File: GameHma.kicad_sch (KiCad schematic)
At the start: 15 parts, among them J1 Screw_Terminal_01x02, J2 Motor_Terminal_01x04, J3 Motor_Terminal_01x04, J4 Motor_Terminal_01x04, J5 Motor_Terminal_01x04, U1 ESP32-DEVKIT-V1, U2 A4988_STEPPER_MOTOR_DRIVER_CA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, U3 A4988_STEPPER_MOTOR_DRIVER_CA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, U4 A4988_STEPPER_MOTOR_DRIVER_CA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, U5 A4988_STEPPER_MOTOR_DRIVER_CA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, U6 SRT_MP1584EN

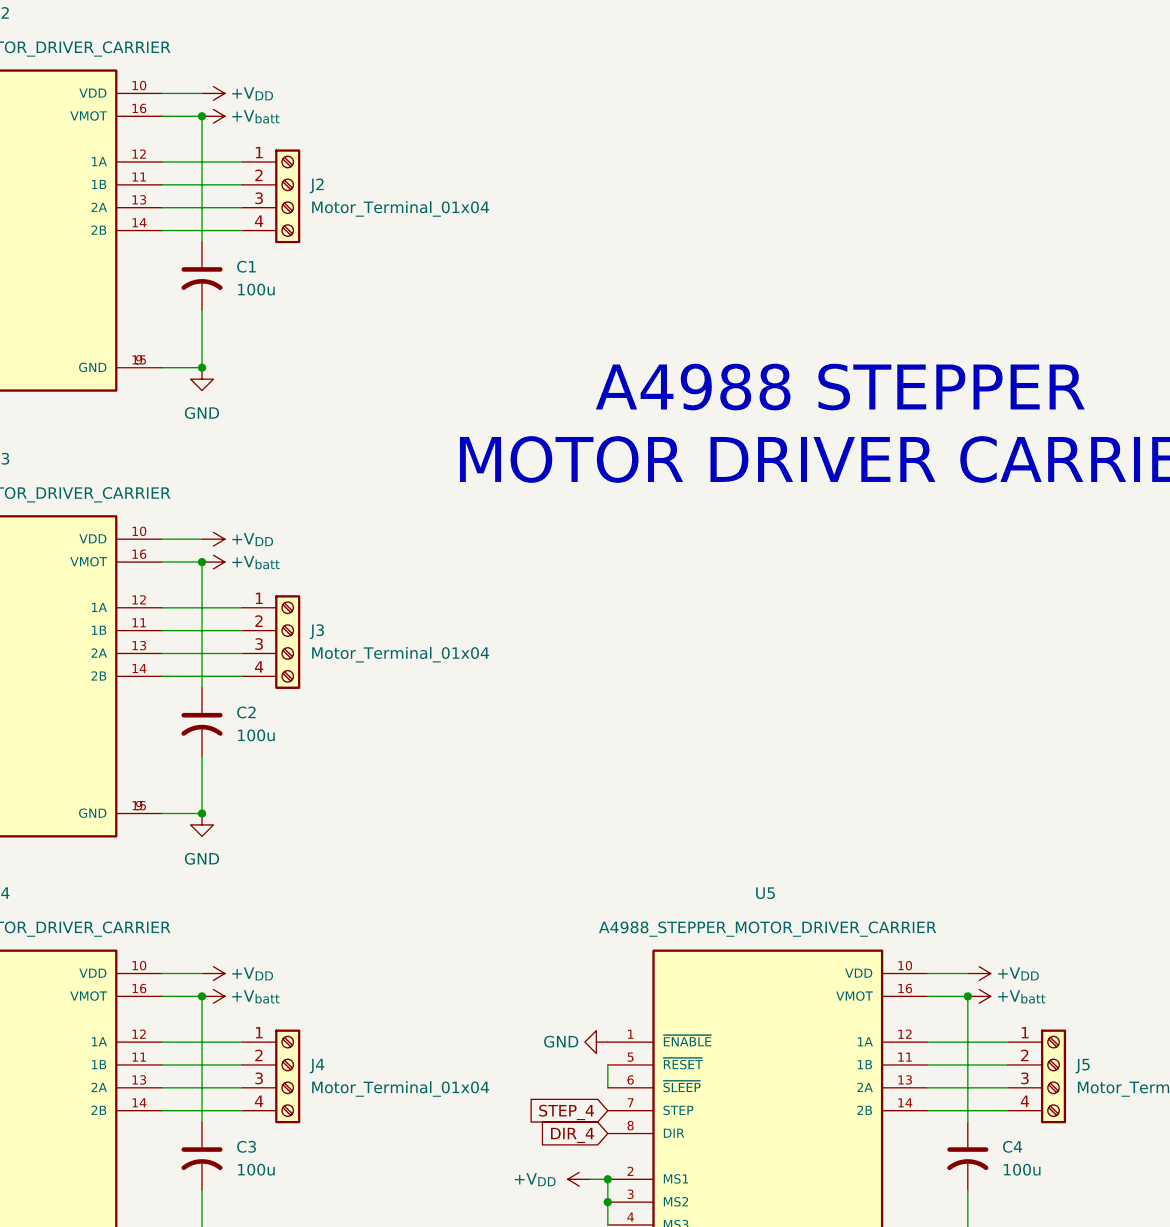
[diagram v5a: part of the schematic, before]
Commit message: swap pin 1A and 1B in each MP1584, organized PCB and initial rout
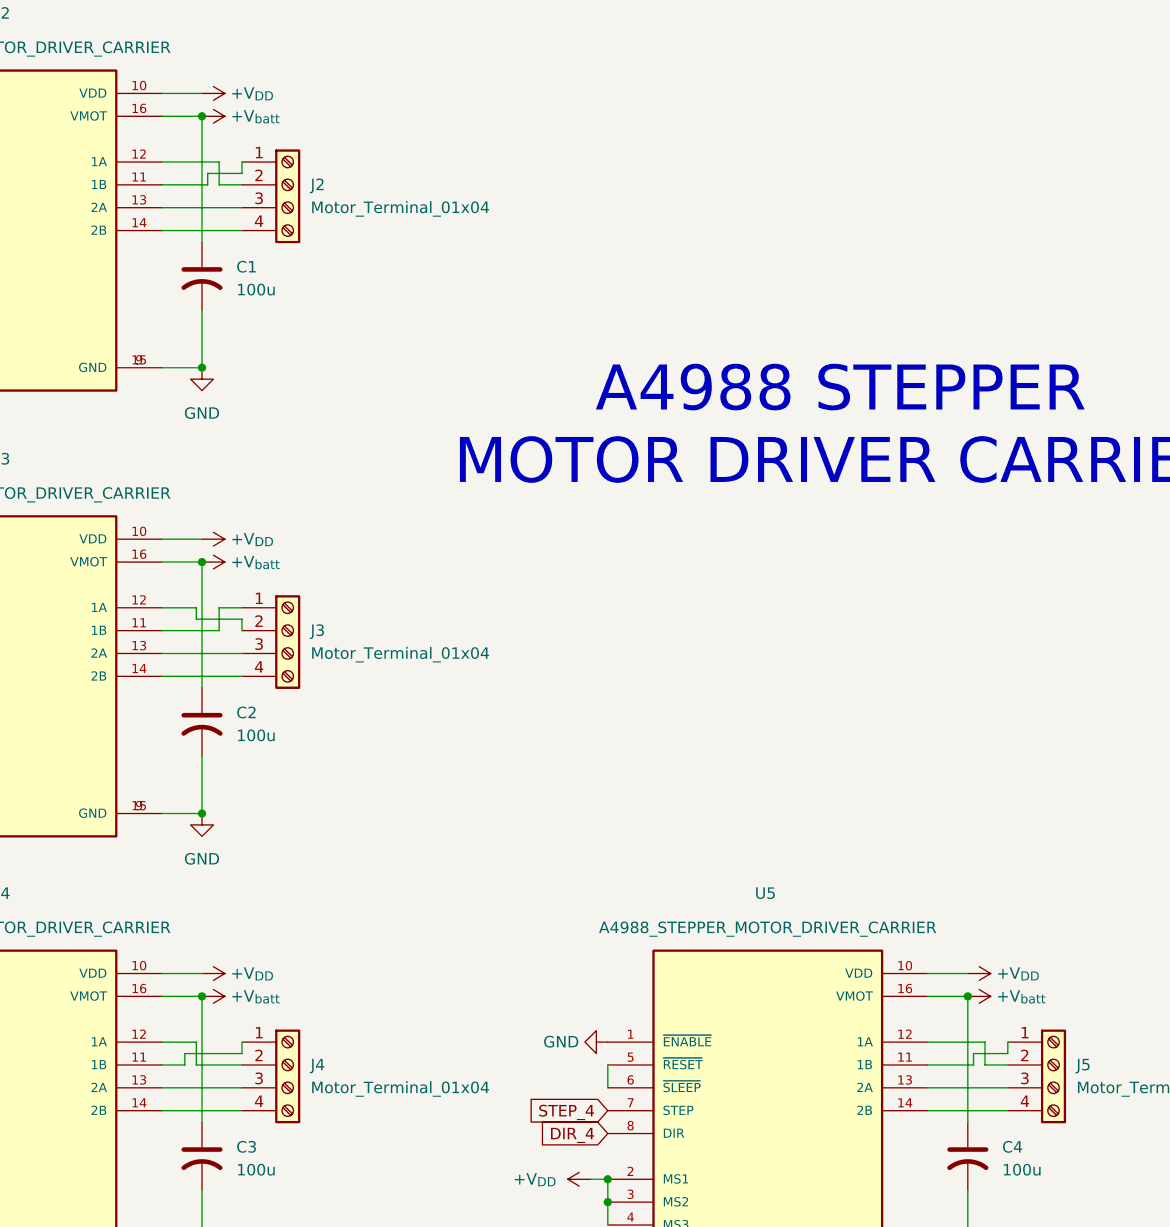
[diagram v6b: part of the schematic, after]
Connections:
- net at J4.1 (Pin_1): now also U4.11 (1B); no longer U4.12 (1A)
- net at J4.2 (Pin_2): now also U4.12 (1A); no longer U4.11 (1B)
- net at U3.11 (1B): now also J3.1 (Pin_1); no longer J3.2 (Pin_2)
- net at U3.12 (1A): now also J3.2 (Pin_2); no longer J3.1 (Pin_1)
- net at U2.11 (1B): now also J2.1 (Pin_1); no longer J2.2 (Pin_2)
- net at U2.12 (1A): now also J2.2 (Pin_2); no longer J2.1 (Pin_1)
- net at J5.1 (Pin_1): now also U5.11 (1B); no longer U5.12 (1A)
- net at J5.2 (Pin_2): now also U5.12 (1A); no longer U5.11 (1B)
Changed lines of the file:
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@@
+	(wire
+		(pts
+			(xy 72.39 135.89) (xy 72.39 134.62)
+		)
+		(stroke
+			(width 0)
+			(type default)
+		)
+	)
 	(wire
 		(pts
@@
 	(wire
 		(pts
-			(xy 148.59 134.62) (xy 157.48 134.62)
-		)
-		(stroke
-			(width 0)
-			(type default)
-		)
-	)
-	(wire
-		(pts
 			(xy 226.06 135.89) (xy 231.14 135.89)
 		)
@@
 	(wire
 		(pts
-			(xy 63.5 137.16) (xy 72.39 137.16)
-		)
-		(stroke
-			(width 0)
-			(type default)
-		)
-	)
-	(wire
-		(pts
 			(xy 248.92 36.83) (xy 256.54 36.83)
 		)
@@
 	(wire
 		(pts
+			(xy 148.59 134.62) (xy 154.94 134.62)
+		)
+		(stroke
+			(width 0)
+			(type default)
+		)
+	)
+	(wire
+		(pts
 			(xy 67.945 143.51) (xy 67.945 129.54)
 		)
@@
 	(wire
 		(pts
-			(xy 63.5 88.9) (xy 72.39 88.9)
-		)
-		(stroke
-			(width 0)
-			(type default)
-		)
-	)
-	(wire
-		(pts
 			(xy 67.945 31.75) (xy 63.5 31.75)
 		)
@@
 	(wire
 		(pts
+			(xy 67.31 137.16) (xy 72.39 137.16)
+		)
+		(stroke
+			(width 0)
+			(type default)
+		)
+	)
+	(wire
+		(pts
 			(xy 226.06 143.51) (xy 231.14 143.51)
 		)
@@
 	(wire
 		(pts
+			(xy 66.04 137.16) (xy 66.04 135.89)
+		)
+		(stroke
+			(width 0)
+			(type default)
+		)
+	)
+	(wire
+		(pts
+			(xy 154.94 134.62) (xy 154.94 137.16)
+		)
+		(stroke
+			(width 0)
+			(type default)
+		)
+	)
+	(wire
+		(pts
+			(xy 157.48 135.89) (xy 157.48 134.62)
+		)
+		(stroke
+			(width 0)
+			(type default)
+		)
+	)
+	(wire
+		(pts
+			(xy 68.58 39.37) (xy 68.58 38.1)
+		)
+		(stroke
+			(width 0)
+			(type default)
+		)
+	)
+	(wire
+		(pts
+			(xy 67.31 86.36) (xy 67.31 87.63)
+		)
+		(stroke
+			(width 0)
+			(type default)
+		)
+	)
+	(wire
+		(pts
 			(xy 26.035 101.6) (xy 27.94 101.6)
 		)
@@
 	(wire
 		(pts
+			(xy 67.31 134.62) (xy 67.31 137.16)
+		)
+		(stroke
+			(width 0)
+			(type default)
+		)
+	)
+	(wire
+		(pts
 			(xy 153.035 151.13) (xy 153.035 157.48)
 		)
@@
 	(wire
 		(pts
-			(xy 63.5 134.62) (xy 72.39 134.62)
+			(xy 72.39 38.1) (xy 72.39 36.83)
+		)
+		(stroke
+			(width 0)
+			(type default)
+		)
+	)
+	(wire
+		(pts
+			(xy 63.5 36.83) (xy 69.85 36.83)
 		)
 		(stroke
@@
 	(wire
 		(pts
+			(xy 148.59 137.16) (xy 153.67 137.16)
+		)
+		(stroke
+			(width 0)
+			(type default)
+		)
+	)
+	(wire
+		(pts
 			(xy 27.94 152.4) (xy 27.94 154.94)
 		)
@@
 	(wire
 		(pts
+			(xy 153.67 137.16) (xy 153.67 135.89)
+		)
+		(stroke
+			(width 0)
+			(type default)
+		)
+	)
+	(wire
+		(pts
+			(xy 69.85 86.36) (xy 72.39 86.36)
+		)
+		(stroke
+			(width 0)
+			(type default)
+		)
+	)
+	(wire
+		(pts
 			(xy 111.125 149.86) (xy 113.03 149.86)
 		)
@@
 	(wire
 		(pts
-			(xy 63.5 39.37) (xy 72.39 39.37)
+			(xy 69.85 88.9) (xy 69.85 86.36)
 		)
 		(stroke
@@
 	(wire
 		(pts
-			(xy 63.5 86.36) (xy 72.39 86.36)
-		)
-		(stroke
-			(width 0)
-			(type default)
-		)
-	)
-	(wire
-		(pts
 			(xy 63.5 44.45) (xy 72.39 44.45)
 		)
@@
 	(wire
 		(pts
+			(xy 68.58 38.1) (xy 72.39 38.1)
+		)
+		(stroke
+			(width 0)
+			(type default)
+		)
+	)
+	(wire
+		(pts
 			(xy 27.94 137.16) (xy 27.94 139.7)
 		)
@@
 	(wire
 		(pts
+			(xy 69.85 39.37) (xy 72.39 39.37)
+		)
+		(stroke
+			(width 0)
+			(type default)
+		)
+	)
+	(wire
+		(pts
+			(xy 153.67 135.89) (xy 157.48 135.89)
+		)
+		(stroke
+			(width 0)
+			(type default)
+		)
+	)
+	(wire
+		(pts
+			(xy 63.5 86.36) (xy 67.31 86.36)
+		)
+		(stroke
+			(width 0)
+			(type default)
+		)
+	)
+	(wire
+		(pts
 			(xy 63.5 29.21) (xy 67.945 29.21)
 		)
@@
 	(wire
 		(pts
+			(xy 63.5 88.9) (xy 69.85 88.9)
+		)
+		(stroke
+			(width 0)
+			(type default)
+		)
+	)
+	(wire
+		(pts
 			(xy 27.94 149.86) (xy 27.94 152.4)
 		)
@@
 	(wire
 		(pts
-			(xy 63.5 36.83) (xy 72.39 36.83)
+			(xy 154.94 137.16) (xy 157.48 137.16)
 		)
 		(stroke
@@
 	(wire
 		(pts
+			(xy 66.04 135.89) (xy 72.39 135.89)
+		)
+		(stroke
+			(width 0)
+			(type default)
+		)
+	)
+	(wire
+		(pts
 			(xy 67.945 81.28) (xy 63.5 81.28)
 		)
@@
 	(wire
 		(pts
+			(xy 67.31 87.63) (xy 72.39 87.63)
+		)
+		(stroke
+			(width 0)
+			(type default)
+		)
+	)
+	(wire
+		(pts
+			(xy 69.85 36.83) (xy 69.85 39.37)
+		)
+		(stroke
+			(width 0)
+			(type default)
+		)
+	)
+	(wire
+		(pts
+			(xy 63.5 39.37) (xy 68.58 39.37)
+		)
+		(stroke
+			(width 0)
+			(type default)
+		)
+	)
+	(wire
+		(pts
+			(xy 72.39 87.63) (xy 72.39 88.9)
+		)
+		(stroke
+			(width 0)
+			(type default)
+		)
+	)
+	(wire
+		(pts
 			(xy 63.5 78.74) (xy 67.945 78.74)
 		)
@@
 	(wire
 		(pts
-			(xy 148.59 137.16) (xy 157.48 137.16)
-		)
-		(stroke
+			(xy 63.5 137.16) (xy 66.04 137.16)
+		)
+		(stroke
+			(width 0)
+			(type default)
+		)
+	)
+	(wire
+		(pts
+			(xy 63.5 134.62) (xy 67.31 134.62)
+		)
+		(stroke

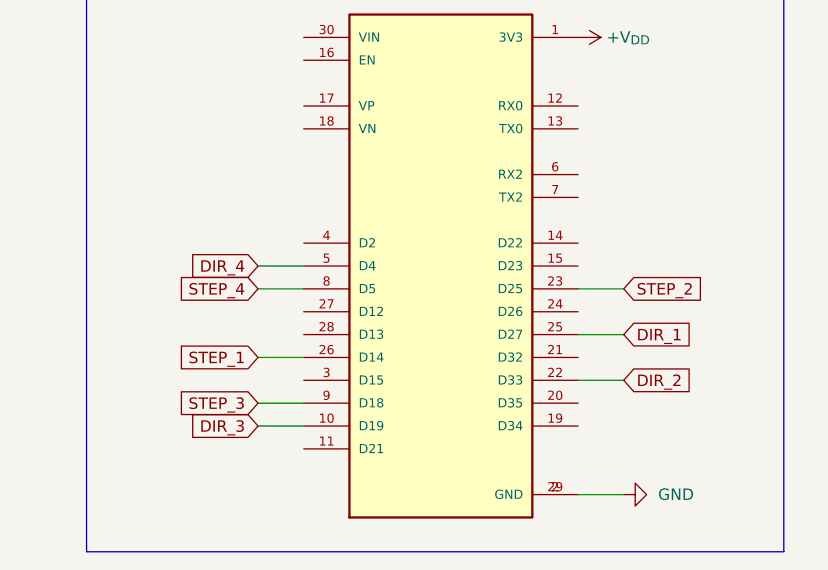
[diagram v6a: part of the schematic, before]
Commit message: edit schematic GPIO pin in ESP32, Rout a PCB lines
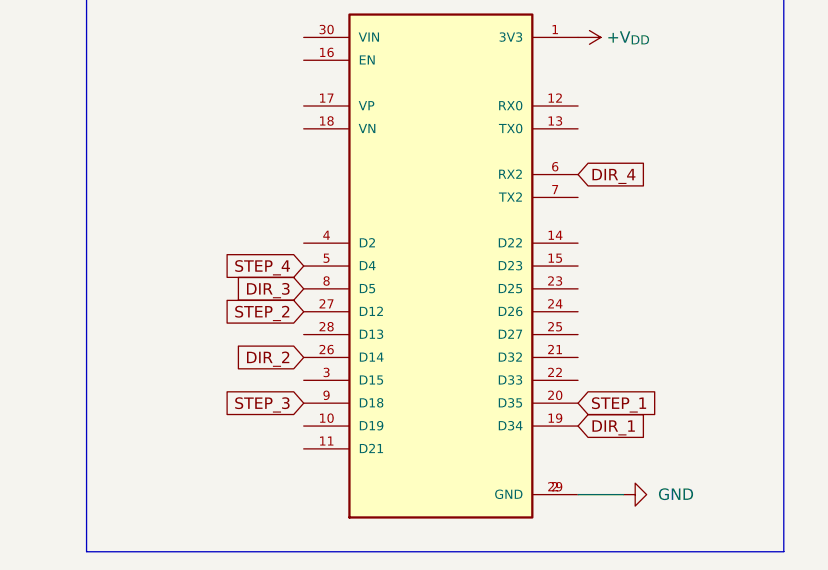
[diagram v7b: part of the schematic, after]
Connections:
- net DIR_1: now also U1.19 (D34); no longer U1.25 (D27)
- net DIR_2: now also U1.26 (D14); no longer U1.22 (D33)
- net DIR_3: now also U1.8 (D5); no longer U1.10 (D19)
- net DIR_4: now also U1.6 (RX2); no longer U1.5 (D4)
- net STEP_1: now also U1.20 (D35); no longer U1.26 (D14)
- net STEP_2: now also U1.27 (D12); no longer U1.23 (D25)
- net STEP_4: now also U1.5 (D4); no longer U1.8 (D5)
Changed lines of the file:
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@@
 	(wire
 		(pts
-			(xy 226.06 135.89) (xy 231.14 135.89)
-		)
-		(stroke
-			(width 0)
-			(type default)
-			(color 0 0 255 1)
-		)
-	)
-	(wire
-		(pts
 			(xy 63.5 157.48) (xy 67.945 157.48)
 		)
@@
 	(wire
 		(pts
-			(xy 226.06 148.59) (xy 231.14 148.59)
-		)
-		(stroke
-			(width 0)
-			(type default)
-			(color 0 0 255 1)
-		)
-	)
-	(wire
-		(pts
 			(xy 148.59 134.62) (xy 154.94 134.62)
 		)
@@
 	(wire
 		(pts
-			(xy 226.06 143.51) (xy 231.14 143.51)
-		)
-		(stroke
-			(width 0)
-			(type default)
-			(color 0 0 255 1)
-		)
-	)
-	(wire
-		(pts
 			(xy 153.035 143.51) (xy 153.035 129.54)
 		)
@@
 	(wire
 		(pts
-			(xy 261.62 146.05) (xy 266.7 146.05)
-		)
-		(stroke
-			(width 0)
-			(type default)
-		)
-	)
-	(wire
-		(pts
 			(xy 72.39 38.1) (xy 72.39 36.83)
 		)
@@
 	(wire
 		(pts
-			(xy 226.06 151.13) (xy 231.14 151.13)
-		)
-		(stroke
-			(width 0)
-			(type default)
-		)
-	)
-	(wire
-		(pts
 			(xy 67.31 87.63) (xy 72.39 87.63)
 		)
@@
 	(wire
 		(pts
-			(xy 226.06 133.35) (xy 231.14 133.35)
-		)
-		(stroke
-			(width 0)
-			(type default)
-		)
-	)
-	(wire
-		(pts
 			(xy 113.03 149.86) (xy 113.03 152.4)
 		)
@@
 	(wire
 		(pts
-			(xy 261.62 135.89) (xy 266.7 135.89)
-		)
-		(stroke
-			(width 0)
-			(type default)
-			(color 0 0 255 1)
-		)
-	)
-	(wire
-		(pts
 			(xy 26.035 52.07) (xy 27.94 52.07)
 		)
@@
 	(wire
 		(pts
-			(xy 261.62 140.97) (xy 266.7 140.97)
-		)
-		(stroke
-			(width 0)
-			(type default)
-		)
-	)
-	(wire
-		(pts
 			(xy 67.945 129.54) (xy 63.5 129.54)
 		)
@@
 	(global_label "DIR_4"
 		(shape input)
-		(at 226.06 133.35 180)
+		(at 261.62 123.19 0)
 		(fields_autoplaced yes)
 		(effects
@@
 				(size 1.27 1.27)
 			)
-			(justify right)
+			(justify left)
 		)
 		(property "Intersheetrefs" "${INTERSHEET_REFS}"
-			(at 217.7529 133.35 0)
+			(at 269.9271 123.19 0)
 			(effects
 				(font
 					(size 1.27 1.27)
 				)
-				(justify right)
+				(justify left)
 				(hide yes)
 			)
@@
 	(global_label "DIR_3"
 		(shape input)
-		(at 226.06 151.13 180)
+		(at 231.14 135.89 180)
 		(fields_autoplaced yes)
 		(effects
@@
 		)
 		(property "Intersheetrefs" "${INTERSHEET_REFS}"
-			(at 217.7529 151.13 0)
+			(at 222.8329 135.89 0)
 			(effects
 				(font
@@
 	(global_label "STEP_3"
 		(shape input)
-		(at 226.06 148.59 180)
+		(at 231.14 148.59 180)
 		(fields_autoplaced yes)
 		(effects
@@
 		)
 		(property "Intersheetrefs" "${INTERSHEET_REFS}"
-			(at 216.3016 148.59 0)
+			(at 221.3816 148.59 0)
 			(effects
 				(font
@@
 	(global_label "DIR_2"
 		(shape input)
-		(at 266.7 146.05 0)
+		(at 231.14 143.51 180)
 		(fields_autoplaced yes)
 		(effects
@@
 				(size 1.27 1.27)
 			)
-			(justify left)
+			(justify right)
 		)
 		(property "Intersheetrefs" "${INTERSHEET_REFS}"
-			(at 275.0071 146.05 0)
+			(at 222.8329 143.51 0)
 			(effects
 				(font
 					(size 1.27 1.27)
 				)
-				(justify left)
+				(justify right)
 				(hide yes)
 			)
@@
 	(global_label "DIR_1"
 		(shape input)
-		(at 266.7 140.97 0)
+		(at 261.62 151.13 0)
 		(fields_autoplaced yes)
 		(effects
@@
 		)
 		(property "Intersheetrefs" "${INTERSHEET_REFS}"
-			(at 275.0071 140.97 0)
+			(at 269.9271 151.13 0)
 			(effects
 				(font
@@
 	(global_label "STEP_4"
 		(shape input)
-		(at 226.06 135.89 180)
+		(at 231.14 133.35 180)
 		(fields_autoplaced yes)
 		(effects
@@
 		)
 		(property "Intersheetrefs" "${INTERSHEET_REFS}"
-			(at 216.3016 135.89 0)
+			(at 221.3816 133.35 0)
 			(effects
 				(font
@@
 	(global_label "STEP_1"
 		(shape input)
-		(at 226.06 143.51 180)
+		(at 261.62 148.59 0)
 		(fields_autoplaced yes)
 		(effects
@@
 				(size 1.27 1.27)
 			)
-			(justify right)
+			(justify left)
 		)
 		(property "Intersheetrefs" "${INTERSHEET_REFS}"
-			(at 216.3016 143.51 0)
+			(at 271.3784 148.59 0)
 			(effects
 				(font
 					(size 1.27 1.27)
 				)
-				(justify right)
+				(justify left)
 				(hide yes)
 			)
@@
 	(global_label "STEP_2"
 		(shape input)
-		(at 266.7 135.89 0)
+		(at 231.14 138.43 180)
 		(fields_autoplaced yes)
 		(effects
@@
 				(size 1.27 1.27)
 			)
-			(justify left)
+			(justify right)
 		)
 		(property "Intersheetrefs" "${INTERSHEET_REFS}"
-			(at 276.4584 135.89 0)
+			(at 221.3816 138.43 0)
 			(effects
 				(font
 					(size 1.27 1.27)
 				)
-				(justify left)
+				(justify right)
 				(hide yes)
 			)
